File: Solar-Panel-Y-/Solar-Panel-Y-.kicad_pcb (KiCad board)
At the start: 6 copper layers, 64 x 58 mm, 85 parts, among them J1 FTS-105-01-L-DV-A, J2 BM02B-SRSS-TB, Q1 BSS138DWQ-7, Q2 MBT2222ADW1T1, Q3 BSS138DWQ-7, Q4 MBT2222ADW1T1, SW1 SW_SPDT, SW2 SW_SPDT, U1 BQ25570RGRR, U2 TSL2561

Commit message: Finished Y- 4 Layer Board
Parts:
- moved U2 45.0 mm to (122.5, 78.2)
- moved R1 41.1 mm to (121.1, 77.7)
- moved C1 40.8 mm to (122.0, 78.3)
- moved R2 40.5 mm to (121.1, 78.8)
- moved R17 13.9 mm to (122.0, 72.0)
- moved R12 13.9 mm to (122.0, 70.1)
- moved R18 13.8 mm to (121.0, 72.0)
- moved R13 13.8 mm to (121.0, 70.1)
- moved D3 12.5 mm to (108.3, 64.6), turned to -90 degrees
- moved Ref** 1.48 mm to (121.3, 90.5)
- moved Q2 0.99 mm to (90.1, 58.5)
- moved R25 0.99 mm to (90.7, 61.5)
- moved R21 0.99 mm to (86.5, 61.5)
- moved R24 0.99 mm to (87.6, 61.5)
- moved Q4 0.99 mm to (90.1, 67.0)
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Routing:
- net /coil: track 15486.9 -> 14547.6 mm
- net SCL_LS: track 16.6 -> 60.8 mm
- net SDA_LS: track 28.5 -> 49.0 mm
- net +3V3: track 22.6 -> 14.2 mm
- net Net-(R1-Pad1): track 9.56 -> 2.15 mm
- net COIL_P: track 8.83 -> 13.8 mm
- net Net-(D3-Pad1): track 14.3 -> 9.95 mm, vias 1 -> 2
- net COIL_N: track 13.0 -> 15.8 mm
- net SCL3: track 32.6 -> 33.8 mm
- net BATT_P_SW: track 65.6 -> 66.4 mm
- net BATT_N_SW: track 48.7 -> 49.5 mm
- net SDA3: track 37.0 -> 37.5 mm
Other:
- outline, holes or cut-outs redrawn
- board text added: "1.BATT_N_SW 3.BATT_P 5.GND 7.COIL_P 9.COIL_N"
- board text added: "2.BATT_P_SW 4.3V3 6.SCL3 8.SDA3 10.VUSB"
- board text added: "Rev B/02"
- board text removed: "Cable Pinout 1.BATT_N_SW 2.BATT_P_SW 3.BATT_P 4.3V3 5.GND 6.SCL3 7.COIL_P 8.SDA3 9.COIL_N 10.VUSB"
- board text removed: "v05"

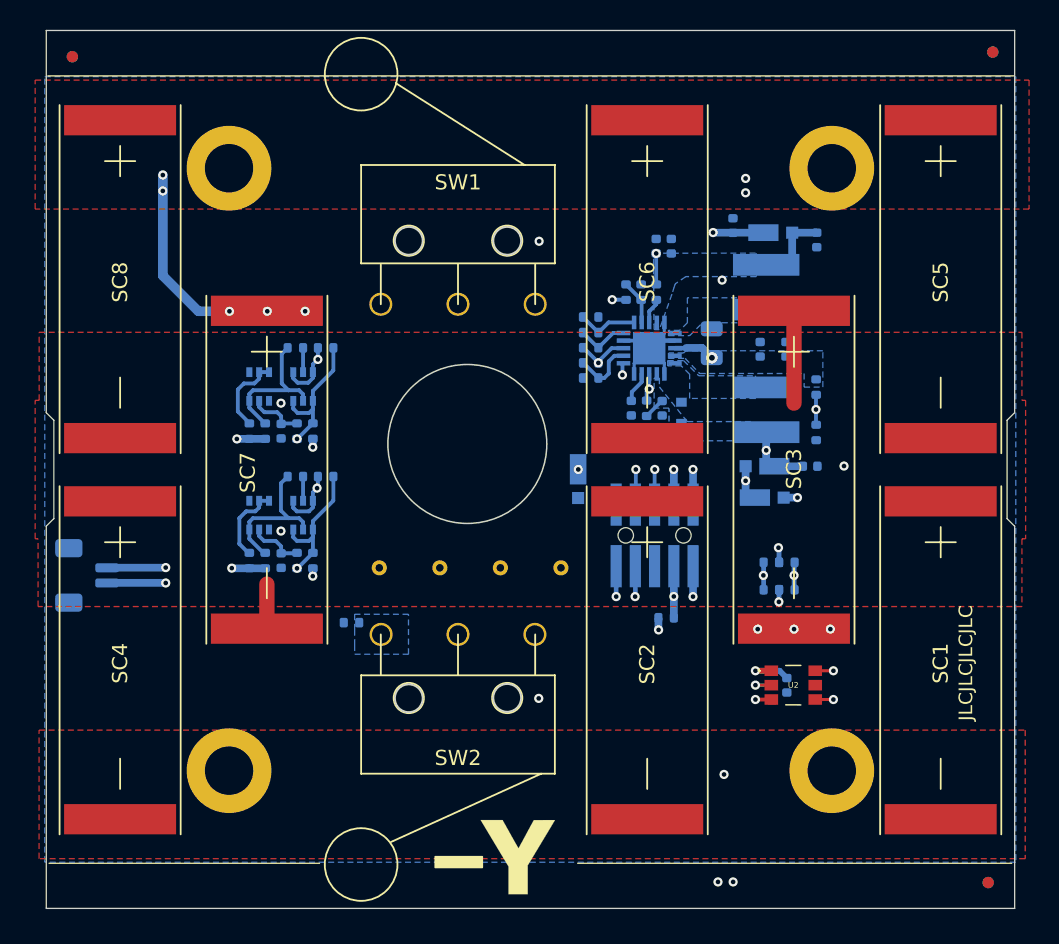
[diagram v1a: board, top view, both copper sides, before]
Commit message: Finish 6 Layer panel versions
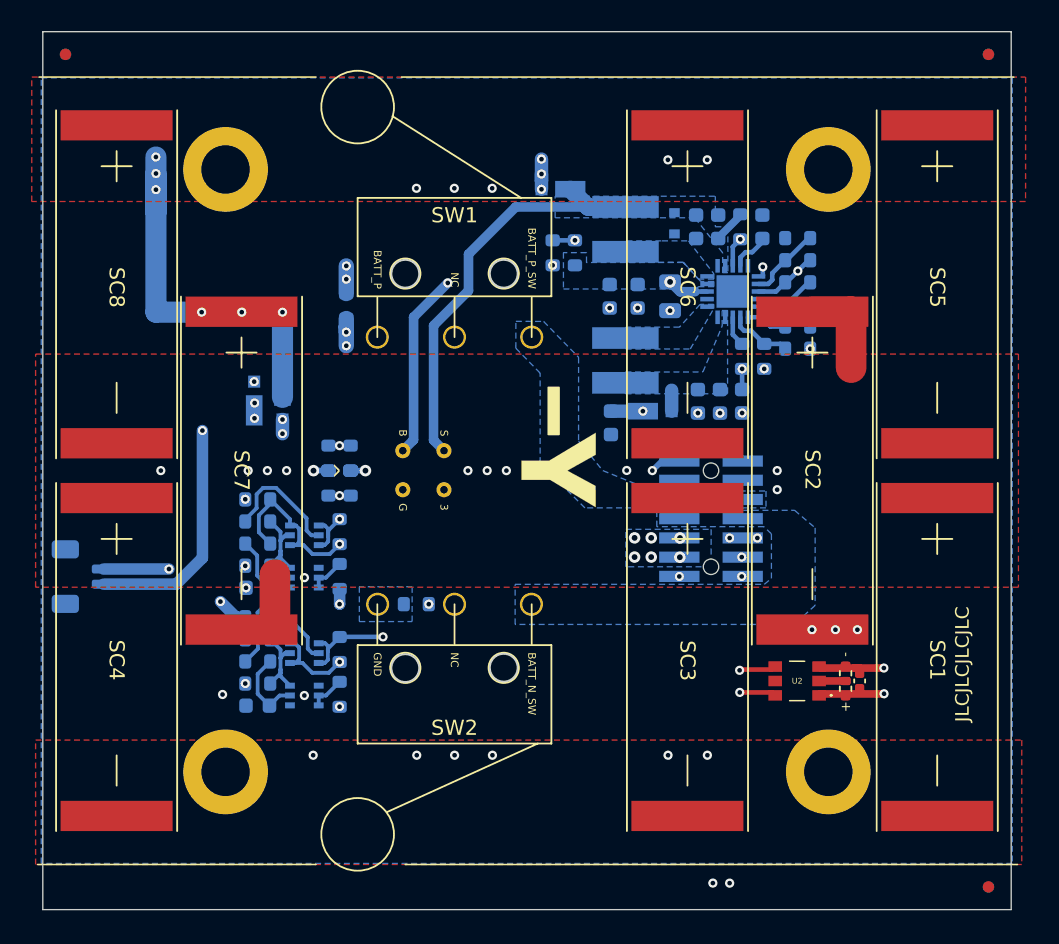
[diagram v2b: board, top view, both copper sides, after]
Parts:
- removed the Ref** at (98.3, 83.9)
- removed TP1, TP2, TP3, TP4: TP, TestPoint:TestPoint_THTPad_D1.0mm_Drill0.5mm
- added 3: TP, TestPoint:TestPoint_THTPad_D1.0mm_Drill0.5mm, B.Cu at (99.4, 65.3)
- added B: TP, TestPoint:TestPoint_THTPad_D1.0mm_Drill0.5mm, B.Cu at (96.7, 62.8)
- added G: TP, TestPoint:TestPoint_THTPad_D1.0mm_Drill0.5mm, B.Cu at (96.7, 65.3)
- added Ref**: Val**, custom-footprints:pycubed_mini_half, B.Cu at (104.4, 85.7)
- added S: TP, TestPoint:TestPoint_THTPad_D1.0mm_Drill0.5mm, B.Cu at (99.4, 62.8)
- C1, R1, R2: moved to F.Cu
- C10, C11, C12, C13, C2, C3, C4, C6, C7, C8, C9: footprint Capacitor_SMD:C_0402_1005Metric -> Capacitor_SMD:C_0603_1608Metric
- J1: value FTS-105-01-L-DV-A -> FTS-107-01-X-DV-A; footprint batteryboard:FTS-105-XX-YY-DV-A -> batteryboard:SAMTEC-FTS-107-01-X-DV-A
- R10, R11, R12, R13, R16, R17, R18, R3, R5, R6, R7, R8, R9: footprint Resistor_SMD:R_0402_1005Metric -> Resistor_SMD:R_0603_1608Metric
- R14, R15: value 0 -> DNI; footprint Resistor_SMD:R_0402_1005Metric -> Resistor_SMD:R_0603_1608Metric
- R19: renamed from R22; value 0 -> DNI; footprint Resistor_SMD:R_0402_1005Metric -> Resistor_SMD:R_0603_1608Metric
- R20: renamed from R23; value 0 -> DNI; footprint Resistor_SMD:R_0402_1005Metric -> Resistor_SMD:R_0603_1608Metric
- R21: renamed from R4; footprint Resistor_SMD:R_0402_1005Metric -> Resistor_SMD:R_0603_1608Metric
- R22: renamed from R21; footprint Resistor_SMD:R_0402_1005Metric -> Resistor_SMD:R_0603_1608Metric
- R23: renamed from R24; footprint Resistor_SMD:R_0402_1005Metric -> Resistor_SMD:R_0603_1608Metric
- R24: renamed from R25; footprint Resistor_SMD:R_0402_1005Metric -> Resistor_SMD:R_0603_1608Metric
- R25: renamed from R26; footprint Resistor_SMD:R_0402_1005Metric -> Resistor_SMD:R_0603_1608Metric
- R26: renamed from R27; footprint Resistor_SMD:R_0402_1005Metric -> Resistor_SMD:R_0603_1608Metric
- R27: renamed from R28; footprint Resistor_SMD:R_0402_1005Metric -> Resistor_SMD:R_0603_1608Metric
- R28: renamed from R29; footprint Resistor_SMD:R_0402_1005Metric -> Resistor_SMD:R_0603_1608Metric
- R29: renamed from R30; footprint Resistor_SMD:R_0402_1005Metric -> Resistor_SMD:R_0603_1608Metric
- R30: renamed from R31; footprint Resistor_SMD:R_0402_1005Metric -> Resistor_SMD:R_0603_1608Metric
- R31: renamed from R20; footprint Resistor_SMD:R_0402_1005Metric -> Resistor_SMD:R_0603_1608Metric
- R4: renamed from R19; footprint Resistor_SMD:R_0402_1005Metric -> Resistor_SMD:R_0603_1608Metric
- SW1: value SW_SPDT -> D2F-L2-A1
- SW2: value SW_SPDT -> D2F-L2-A
- moved D4 32.5 mm to (88.7, 59.5), turned to -90 degrees
- moved R12 31.1 mm to (91.8, 63.2), turned to 90 degrees
- moved R17 30.1 mm to (93.2, 63.2), turned to 90 degrees
- moved R13 29.7 mm to (91.8, 64.9), turned to 90 degrees
- moved R3 29.5 mm to (92.9, 53.2), turned to 90 degrees
- moved R18 28.7 mm to (93.2, 64.9), turned to 90 degrees
- moved D5 22.7 mm to (107.1, 45.5)
- moved D3 22.0 mm to (86.9, 59.5), turned to 90 degrees
- moved R15 21.1 mm to (106.6, 49.7)
- moved R16 18.2 mm to (108.0, 49.7), turned to 90 degrees
- moved Ref** 18.0 mm to (106.0, 81.1), turned to -90 degrees
- moved C2 17.5 mm to (116.1, 48.0), turned to -90 degrees
- moved R6 16.5 mm to (122.8, 48.7)
- moved C11 15.3 mm to (110.4, 60.9), turned to -90 degrees
- moved R5 15.3 mm to (122.8, 50.2)
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- renumbered SC3 to SC2, SC2 to SC3
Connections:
- J1 pad 1: BATT_N_SW -> unconnected-(J1-Pad1)
- J1 pad 10: VUSB -> BATT_P
- J1 pad 2: BATT_P_SW -> COIL_P
- J1 pad 3: BATT_P -> GND
- J1 pad 4: +3V3 -> GND
- J1 pad 5: GND -> BATT_P_SW
- J1 pad 6: SCL3 -> BATT_P_SW
- J1 pad 7: COIL_P -> BATT_N_SW
- J1 pad 8: SDA3 -> BATT_N_SW
- J1 pad 9: COIL_N -> +3V3
- J2 pad 1: BATT_P_SW -> BATT_N_SW
- J2 pad 2: BATT_N_SW -> BATT_P_SW
- Q2 pad 1: SCL3 -> SCL
- Q2 pad 3: SCL3 -> SCL
- Q4 pad 1: SDA3 -> SDA
- Q4 pad 3: SDA3 -> SDA
- R19 pad 2: SCL3 -> SCL
- R20 pad 2: SDA3 -> SDA
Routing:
- net /coil: track 14547.6 -> 14929.4 mm
- net BATT_P: track 47.3 -> 2.15 mm, vias 1 -> 8
- net SDA3: track 37.5 -> 0.00 mm, vias 2 -> 0
- net SDA: track 0.00 -> 35.1 mm, vias 0 -> 2
- net SCL3: track 33.8 -> 0.00 mm, vias 2 -> 0
- net SCL: track 0.00 -> 32.7 mm, vias 0 -> 2
- net BATT_P_SW: track 66.4 -> 43.0 mm, vias 2 -> 1
- net VBAT: track 39.4 -> 16.8 mm, vias 2 -> 4
- net BATT_N_SW: track 49.5 -> 30.6 mm, vias 2 -> 1
- net COIL_P: track 13.8 -> 32.6 mm
- net SCL_LS: track 60.8 -> 49.6 mm
- net COIL_N: track 15.8 -> 26.6 mm
- net /VSOLAR_FULL: track 39.0 -> 30.6 mm, vias 8 -> 9
- net Net-(Q2-Pad2): track 1.60 -> 8.03 mm
- net VSOLAR: track 25.8 -> 32.1 mm, vias 1 -> 0
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- added copper zone on In3.Cu, net +3V3
- added copper zone on B.Cu, net BATT_N_SW
- added copper zone on B.Cu, net BATT_P
- added copper zone on In2.Cu, net BATT_P
- added copper zone on B.Cu, net BATT_P_SW
- added copper zone on In1.Cu, net GND
- added copper zone on In2.Cu, net VBAT
- removed copper zone on In1.Cu, net +3V3
- removed copper zone on In2.Cu, net +3V3
- removed copper zone on In3.Cu, net GND
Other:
- outline, holes or cut-outs redrawn
- board text added: "1.NC 3.GND 5.BATT_P_SW 7.BATT_N_SW 9.3V3 11.SDA 13.SCL"
- board text added: "2.COIL_P 4.GND 6.BATT_P_SW 8.BATT_N_SW 10.BATT_P 12.BATT_P 14.COIL_N"
- board text added: "BATT_N_SW"
- board text added: "BATT_P"
- board text added: "BATT_P_SW"
- board text added: "NC"
- board text added: "Rev B2/01"
- board text added: "^"
- board text added: "⊗"
- board text added: "⊙"
- board text removed: "1.BATT_N_SW 3.BATT_P 5.GND 7.COIL_P 9.COIL_N"
- board text removed: "2.BATT_P_SW 4.3V3 6.SCL3 8.SDA3 10.VUSB"
- board text removed: "Rev B/02"
